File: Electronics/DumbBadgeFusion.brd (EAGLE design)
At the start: 163.5 x 113 mm, 148 parts, among them IC1 74245MTC, IC2 74245MTC, IC3 74245MTC, SW1 SPST_TACT-KMR2, T1 MMUN2133LT1G, U1 ATSAMD21J18A-AUT, U2 TPS61090RSAR, U3 MCP73871, U4 FAN5333BSX, U5 TDP3E001DRLR-SOT-23-5SOT-23-5, U6 MAX3232, X4 NX3215SA-32.768K-STD-MUA-8

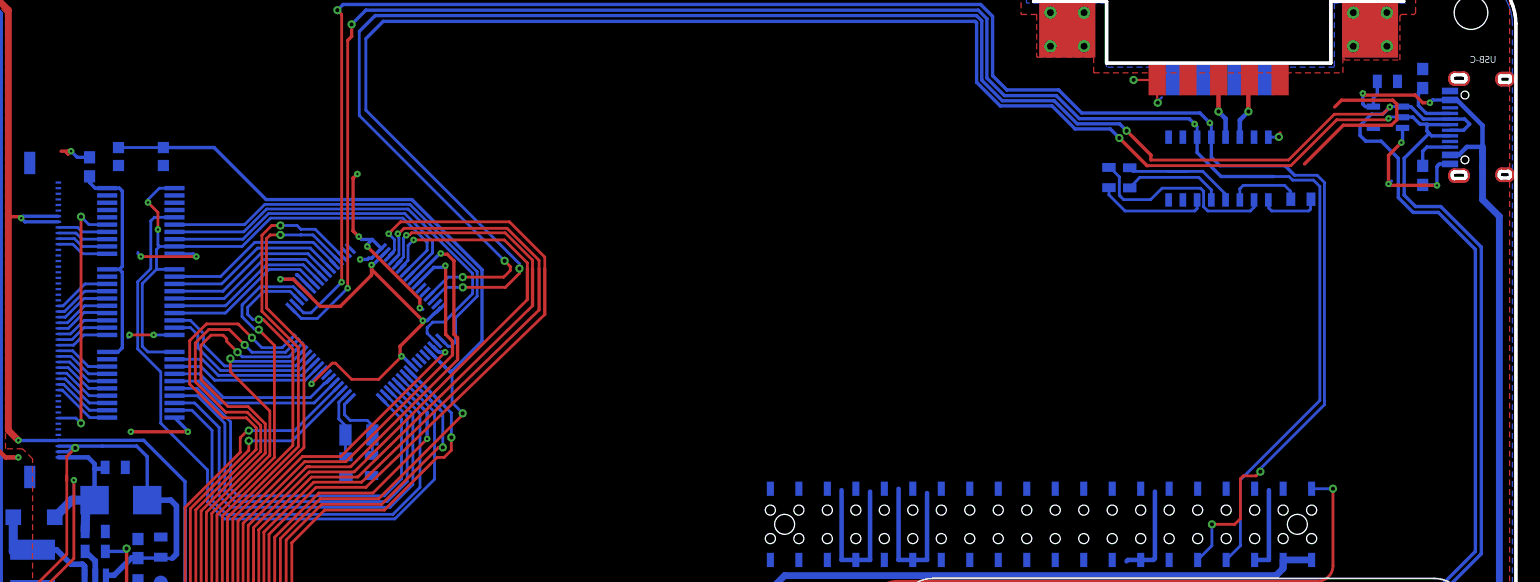
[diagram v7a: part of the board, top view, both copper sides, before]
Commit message: Fixed footprint for ESD, D1
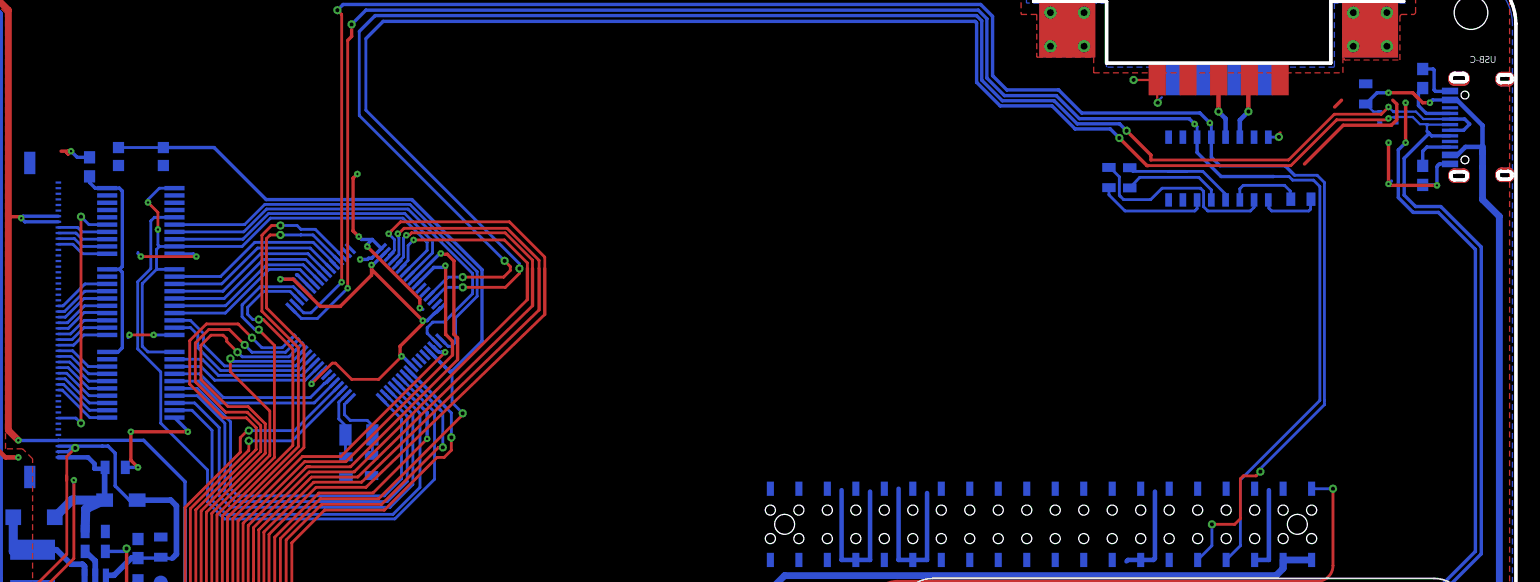
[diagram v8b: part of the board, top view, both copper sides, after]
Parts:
- D1: device microbuilder:SMADIODE -> diode:SOD323-W
- U5: value TDP3E001DRLR-SOT-23-5SOT-23-5 -> TPD3E001SOT5; device USBC:SOT-23-5 -> FPC:SOT(5)
- moved C1 2.23 mm to (150.1, 101.8), turned to 90 degrees
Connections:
- net GND: now also U5.IO3; no longer U5.3
- net USB_N: now also U5.IO1; no longer U5.1
- net USB_P: now also U5.IO2; no longer U5.2
- net VBUS: now also U5.VCC; no longer U5.5
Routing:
- net GND: track 182.3 -> 189.6 mm, vias 40 -> 41
- net 3V3: track 221.6 -> 217.0 mm
- net USB_N: track 264.7 -> 262.2 mm, vias 4 -> 6
- net VBUS: track 402.3 -> 400.0 mm
- net +24V: track 34.8 -> 35.4 mm
- net LEDK: track 54.2 -> 53.6 mm
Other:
- outline, holes or cut-outs redrawn
